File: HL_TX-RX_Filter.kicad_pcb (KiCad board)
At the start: 2 copper layers, 100 x 100 mm, 184 parts, among them J1 To Antenna, J2 From Tx, J3 ICSP, J4 Data In, J5 SCL SDA, J6 To Rx in, Q1 2N7002, Q2 2N7002, Q3 2N7002, Q4 2N7002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

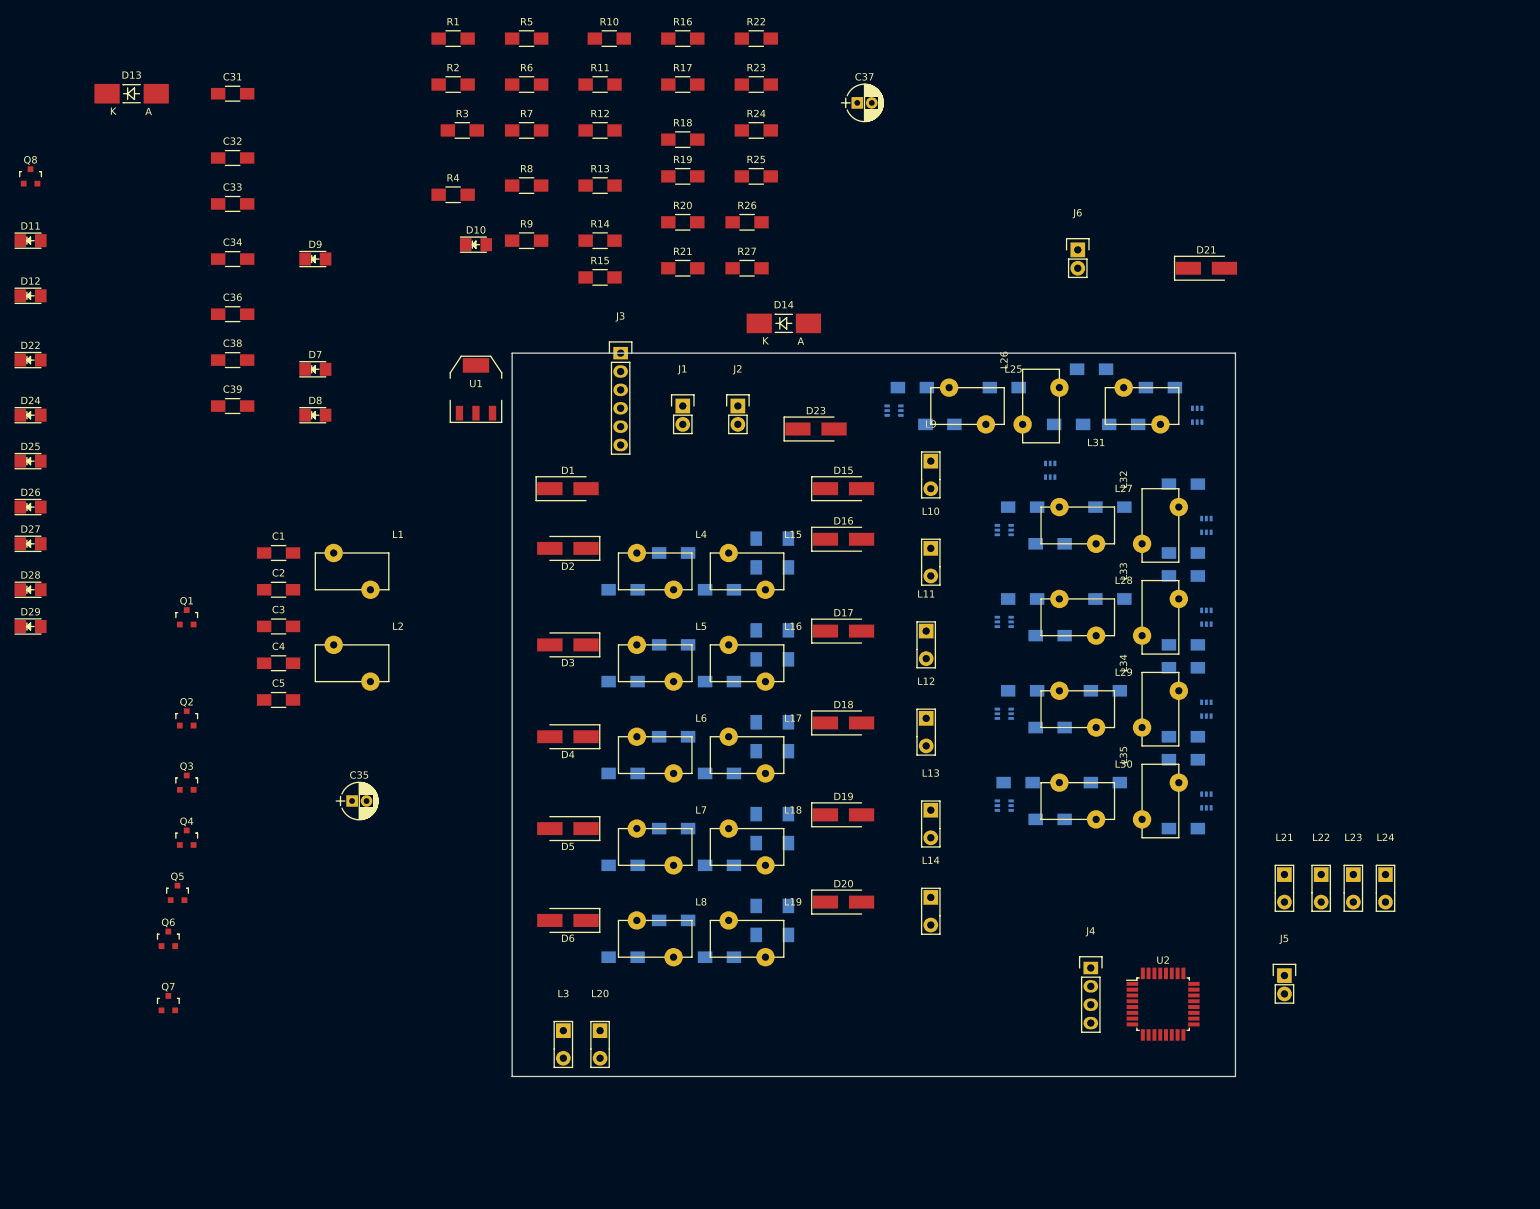
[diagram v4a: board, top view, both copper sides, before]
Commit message: More progress with Tx filter board layout
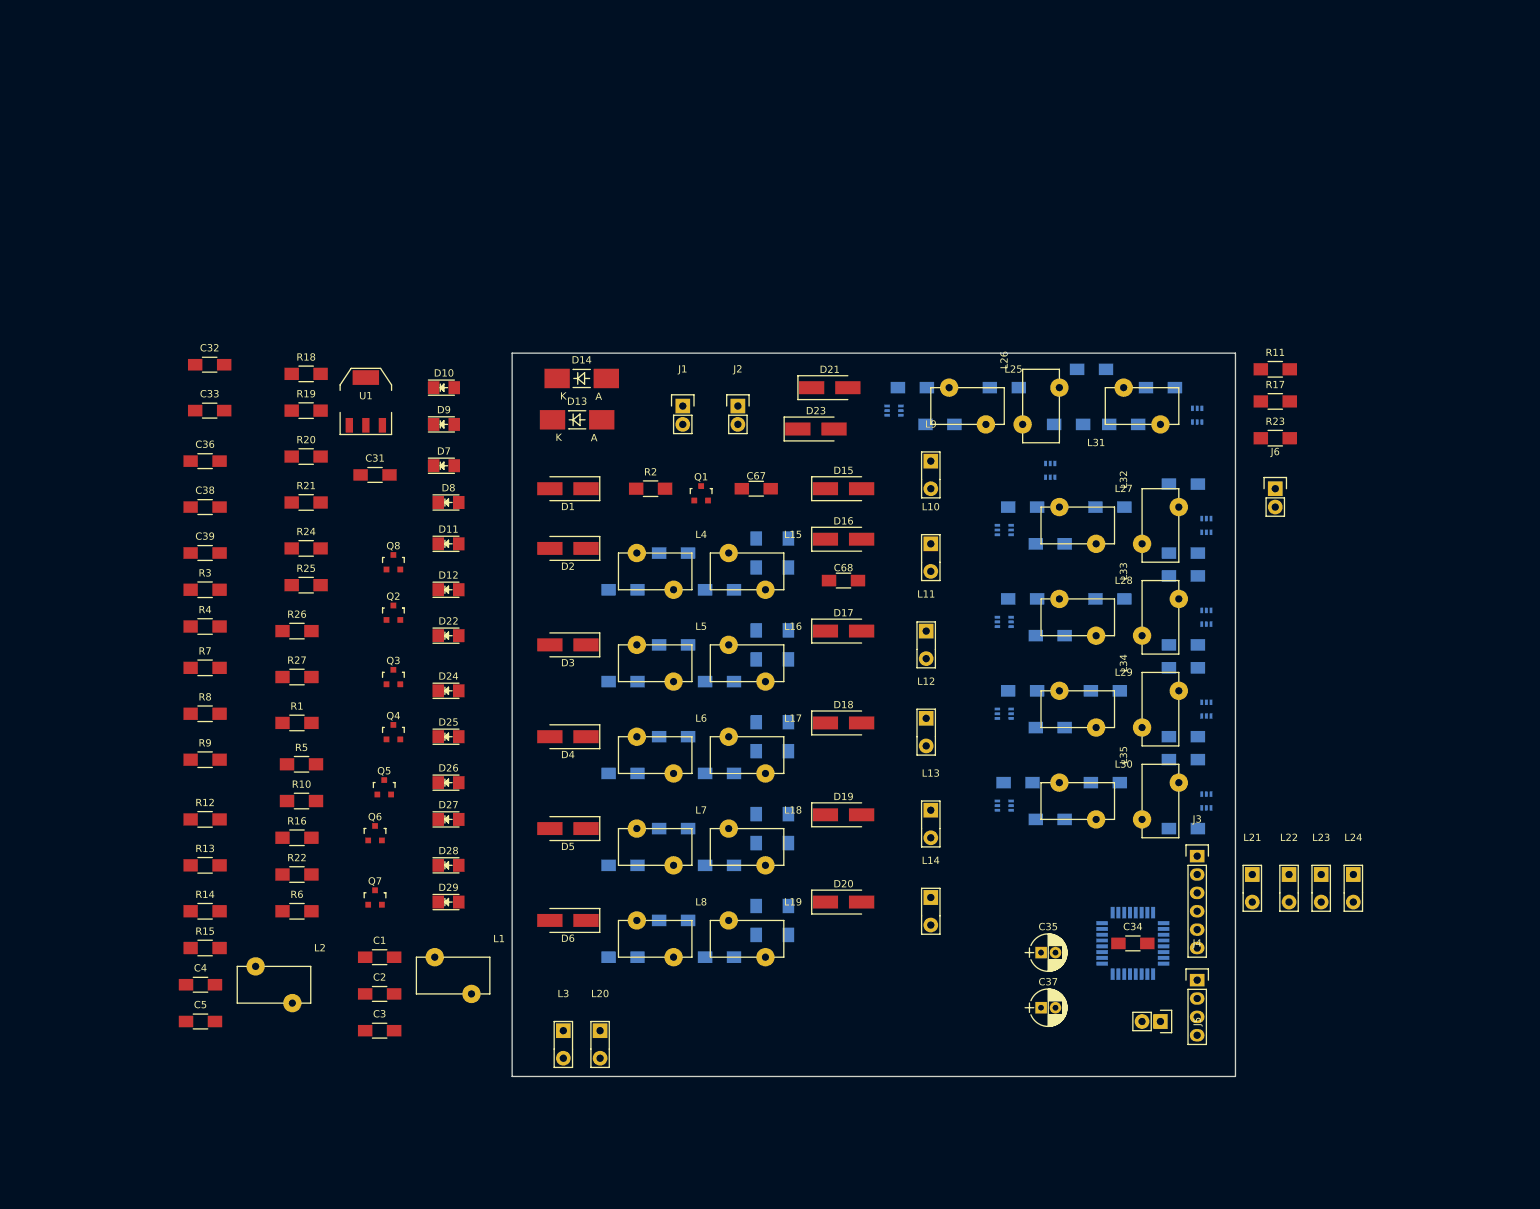
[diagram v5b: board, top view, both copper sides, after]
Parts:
- added C67: .1u, Capacitors_SMD:C_1206_HandSoldering, F.Cu at (158.8, 78.7)
- added C68: .1u, Capacitors_SMD:C_1206_HandSoldering, F.Cu at (170.8, 91.4)
- R10, R9: value R -> 100k
- U2: moved to B.Cu
- moved C34 156.3 mm to (210.8, 141.6)
- moved R22 131.9 mm to (95.2, 132.1)
- moved C37 127.6 mm to (198.1, 150.5)
- moved R16 122.7 mm to (95.2, 127.0)
- moved R6 118.6 mm to (95.2, 137.2)
- moved R10 113.7 mm to (95.9, 121.9)
- moved R12 109.8 mm to (82.5, 124.5)
- moved R13 108.7 mm to (82.5, 130.8)
- moved R15 107.6 mm to (82.5, 142.2)
- moved R14 107.6 mm to (82.5, 137.2)
- moved J3 105.8 mm to (219.7, 129.5)
- moved R5 105.0 mm to (95.9, 116.8)
- moved R11 101.3 mm to (230.5, 62.2)
- moved C35 97.5 mm to (198.1, 142.9)
- moved R1 97.0 mm to (95.2, 111.1)
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
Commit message: Further progress on layout
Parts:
- added C69: .1u, Capacitors_SMD:C_1206_HandSoldering, F.Cu at (160.7, 106.7)
- added C70: .1u, Capacitors_SMD:C_1206_HandSoldering, B.Cu at (163.8, 121.3)
- added C71: .1u, Capacitors_SMD:C_1206_HandSoldering, B.Cu at (163.8, 138.4)
- added C72: .1u, Capacitors_SMD:C_1206_HandSoldering, B.Cu at (162.6, 154.9)
- added J10: CNR4, Connectors:1pin, F.Cu at (220.3, 155.6)
- added J7: CNR1, Connectors:1pin, F.Cu at (129.5, 64.1)
- added J8: CNR3, Connectors:1pin, F.Cu at (221.0, 64.1)
- added J9: CNR2, Connectors:1pin, F.Cu at (129.5, 155.6)
- C34, C36, C39, C67, C68, D23, Q1, Q2, Q3, Q4, Q5, Q6, R2, R9: moved to B.Cu
- D13, D14: footprint Diodes_SMD:MELF_Handsoldering -> Diodes_SMD:D_MiniMELF_Handsoldering
- U2: moved to F.Cu
- moved C38 124.5 mm to (207.0, 79.4)
- moved R20 100.5 mm to (196.8, 79.4)
- moved C39 90.1 mm to (171.4, 73.0)
- moved C36 87.0 mm to (168.9, 64.8)
- moved R19 83.9 mm to (180.3, 63.5)
- moved R9 83.6 mm to (154.9, 74.3), turned to 180 degrees
- moved L24 82.0 mm to (178.4, 79.4)
- moved R10 79.0 mm to (168.3, 90.2), turned to 180 degrees
- moved R7 77.6 mm to (142.2, 153.0)
- moved Q8 75.0 mm to (183.5, 87.0)
- moved J2 70.3 mm to (87.0, 79.4)
- moved Q6 68.3 mm to (170.8, 148.0), turned to 90 degrees
- moved J1 67.6 mm to (81.9, 78.7)
- moved J5 65.0 mm to (184.8, 94.6)
- moved Q5 64.8 mm to (170.8, 132.7), turned to 90 degrees
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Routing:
- net GND: track 0.00 -> 859.2 mm, vias 0 -> 28
- net Net-(C2-Pad1): track 0.00 -> 43.8 mm, vias 0 -> 5
- net Net-(C32-Pad1): track 0.00 -> 34.6 mm, vias 0 -> 5
- net 3V3: track 0.00 -> 31.9 mm, vias 0 -> 4
- net Net-(C11-Pad2): track 0.00 -> 27.4 mm
- net /T17: track 0.00 -> 25.1 mm, vias 0 -> 1
- net Net-(C38-Pad1): track 0.00 -> 22.5 mm, vias 0 -> 1
- net Net-(C68-Pad1): track 0.00 -> 15.4 mm
- net Net-(C67-Pad1): track 0.00 -> 14.9 mm
- net Net-(U3-Pad3): track 0.00 -> 10.6 mm
- net Net-(D1-Pad1): track 0.00 -> 10.2 mm
- net Net-(C21-Pad2): track 0.00 -> 9.08 mm
- net Net-(C11-Pad1): track 0.00 -> 5.38 mm
- net Net-(C36-Pad2): track 0.00 -> 5.18 mm
- net Net-(D8-Pad2): track 0.00 -> 5.10 mm
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- added copper zone on B.Cu, net GND
- added copper zone on F.Cu, net GND

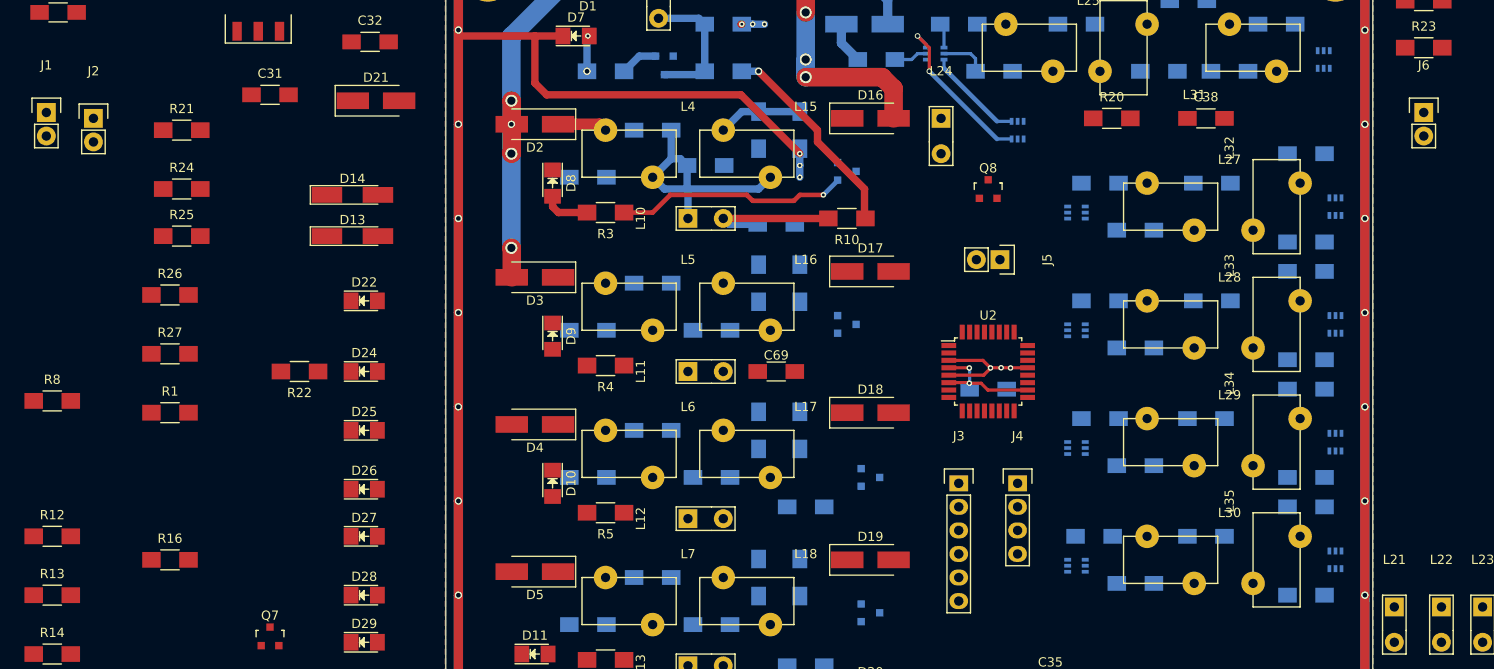
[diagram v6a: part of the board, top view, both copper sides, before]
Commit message: Rearranging pins on microprocessor to better fit layout
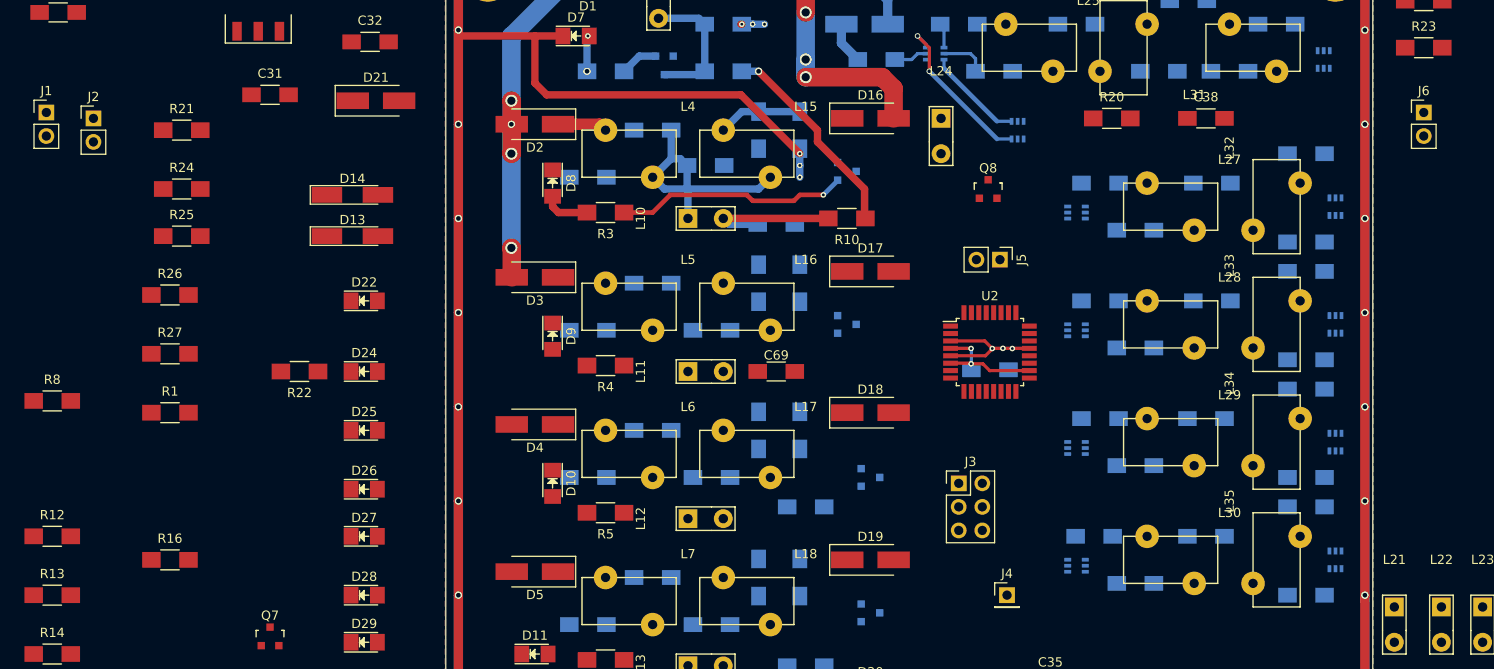
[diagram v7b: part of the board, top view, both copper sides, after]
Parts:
- J1, J2, J5, J6: footprint Pin_Headers:Pin_Header_Straight_1x02 -> Pin_Headers:Pin_Header_Straight_1x02_Pitch2.54mm
- J3: footprint Pin_Headers:Pin_Header_Straight_1x06 -> Pin_Headers:Pin_Header_Straight_2x03_Pitch2.54mm
- J4: value Data In -> Input1; footprint Pin_Headers:Pin_Header_Straight_1x04 -> Pin_Headers:Pin_Header_Straight_1x01_Pitch2.54mm
- moved J4 12.1 mm to (185.5, 130.8)
- moved U2 2.10 mm to (183.7, 104.6)
- moved C34 2.10 mm to (183.7, 106.5)
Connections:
- J3 pad 1: /R4 -> /I3
- J3 pad 3: /R5 -> /I4
- J3 pad 4: /R3 -> /I2
- J4 pad 1: Net-(J4-Pad1) -> /I1
- U2 pad 14: /R2 -> /I1
- U2 pad 15: /R3 -> /I2
- U2 pad 16: /R4 -> /I3
- U2 pad 17: /R5 -> /I4
- U2 pad 23: Net-(J4-Pad1) -> /R5
- U2 pad 24: Net-(J4-Pad2) -> /R4
- U2 pad 25: Net-(J4-Pad3) -> /R3
- U2 pad 26: Net-(J4-Pad4) -> /R2
